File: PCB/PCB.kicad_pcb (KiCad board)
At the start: 2 copper layers, 110 x 100 mm, 53 parts, among them J1 Conn_01x03, J2 Conn_01x02, Q1 2N2907, Q10 TIP32, Q11 BD138, Q12 TIP31, Q13 2N2222, Q2 2N2907, Q3 2N2907, Q4 2N2222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

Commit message: Placmement terminé, demande de go/nogo
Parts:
- moved C6 56.9 mm to (134.0, 141.0), turned to 0 degrees
- moved Q4 41.9 mm to (106.0, 106.0)
- moved R14 39.0 mm to (90.0, 98.0), turned to 0 degrees
- moved RV2 34.4 mm to (100.0, 145.0)
- moved R9 34.2 mm to (80.0, 135.0), turned to 270 degrees
- moved R7 34.0 mm to (63.0, 129.0)
- moved Q6 32.0 mm to (89.0, 130.0)
- moved R16 32.0 mm to (116.0, 80.0), turned to 270 degrees
- moved Q7 32.0 mm to (89.0, 139.0), turned to 90 degrees
- moved C2 31.9 mm to (96.0, 104.0), turned to 270 degrees
- moved HS2 31.6 mm to (131.0, 106.0), turned to 180 degrees
- moved R3 31.4 mm to (84.0, 104.0), turned to 270 degrees
- moved R10 28.3 mm to (101.0, 128.0), turned to 270 degrees
- moved Q12 26.9 mm to (128.0, 110.0), turned to 0 degrees
- moved R8 25.3 mm to (122.0, 132.0)
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
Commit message: C10 corrigé
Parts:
- C10: value 47u -> 470u

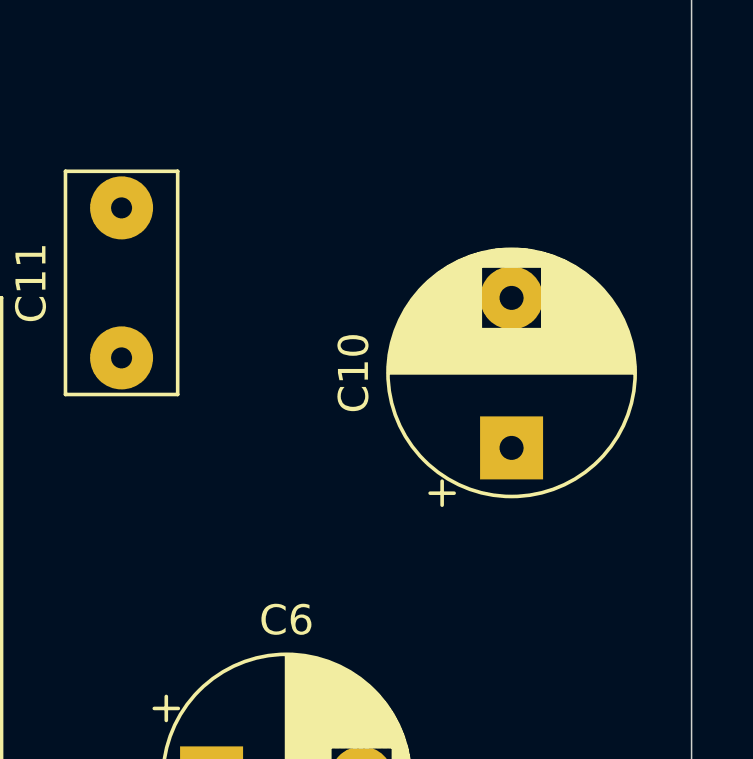
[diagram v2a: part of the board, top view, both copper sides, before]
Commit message: C8 corrigé
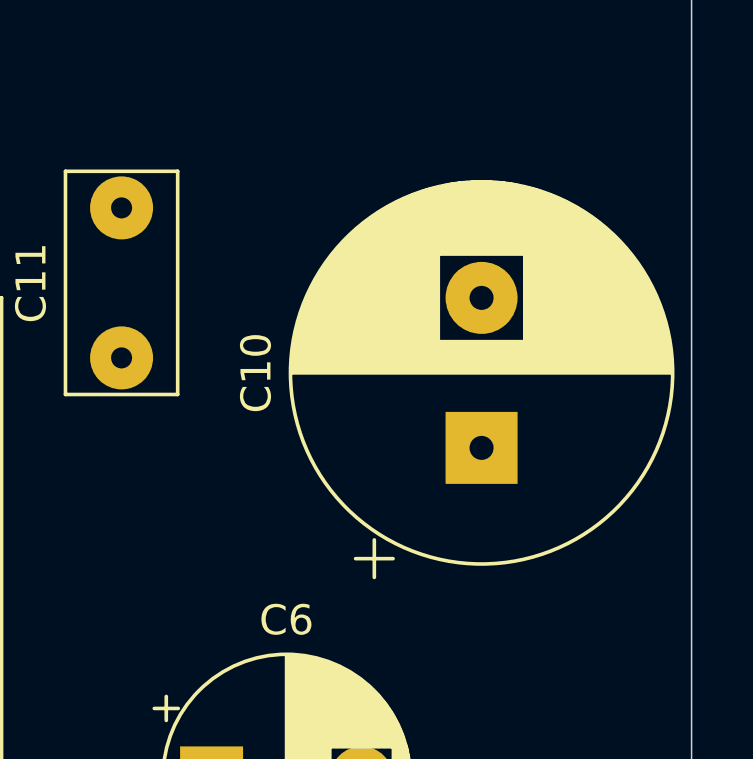
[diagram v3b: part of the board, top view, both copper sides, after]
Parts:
- C10: footprint CmpAmpliAudio:CP_Radial_D8.0mm_P5.00mm -> CmpAmpliAudio:CP_Radial_D12.5mm_P5.00mm
- moved C10 1.00 mm to (143.0, 130.0)

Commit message: routage refait en respectant vos conseils
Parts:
- removed the C8 at (53.0, 56.0)
- moved R15 92.1 mm to (144.8, 133.3), turned to 90 degrees
- moved C7 86.9 mm to (83.8, 143.5), turned to 90 degrees
- moved C4 82.1 mm to (99.1, 141.0), turned to 180 degrees
- moved C11 72.4 mm to (129.5, 54.6), turned to 270 degrees
- moved C10 65.2 mm to (143.5, 64.8), turned to 180 degrees
- moved C5 63.5 mm to (101.6, 128.3), turned to 180 degrees
- moved R14 57.9 mm to (135.9, 133.3), turned to 90 degrees
- moved Q8 56.7 mm to (128.3, 86.4), turned to 0 degrees
- moved R7 49.4 mm to (111.8, 137.2), turned to 90 degrees
- moved RV2 46.5 mm to (92.7, 99.1)
- moved C3 46.3 mm to (88.9, 110.5), turned to 180 degrees
- moved R3 43.4 mm to (44.5, 121.9)
- moved RV1 42.5 mm to (128.3, 97.8), turned to 180 degrees
- moved C6 40.0 mm to (146.1, 102.9), turned to 180 degrees
- moved Q7 39.5 mm to (125.7, 124.5)
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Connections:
- J1 pad 1: +12V -> -12V
- J1 pad 3: -12V -> +12V
- J2 pad 1: Net-(J2-Pad1) -> GND
- J2 pad 2: GND -> Net-(J2-Pad1)

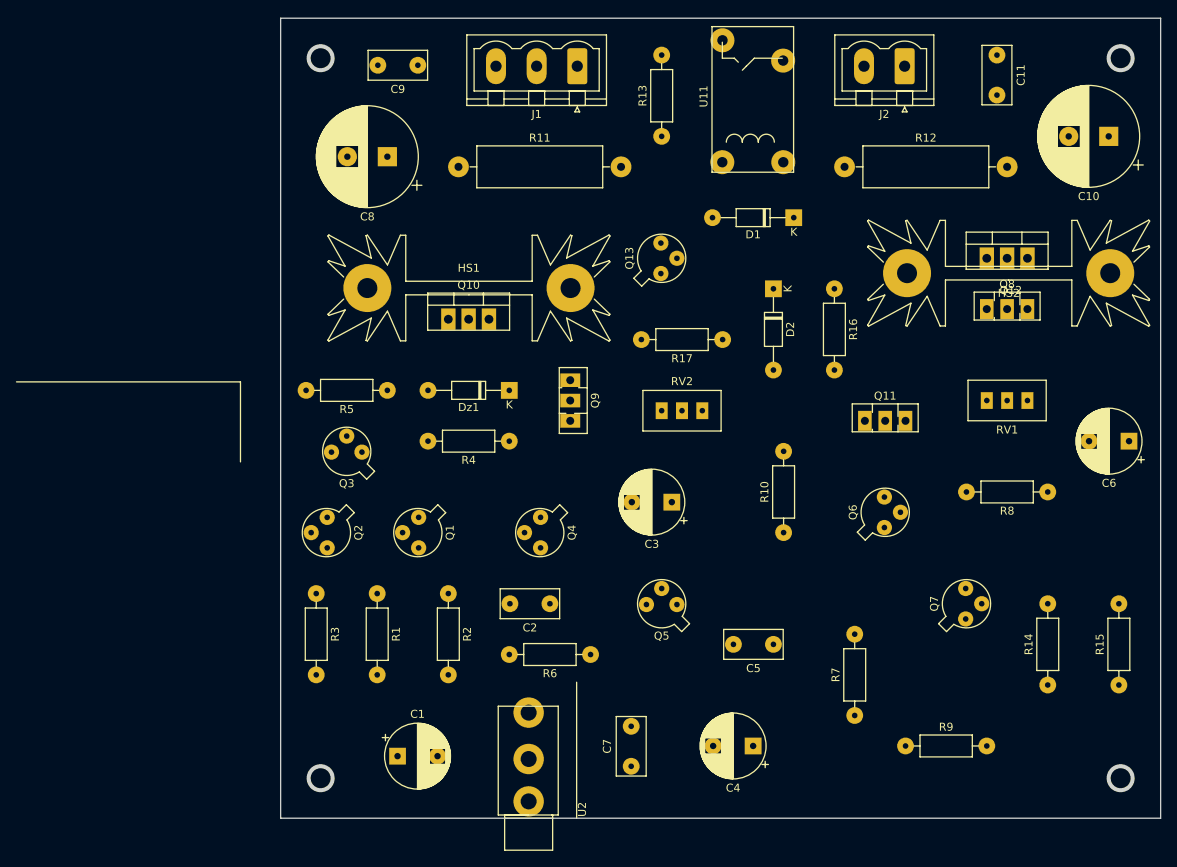
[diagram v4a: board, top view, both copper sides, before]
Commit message: routage terminé en essayant de tenir compte de vos conseils
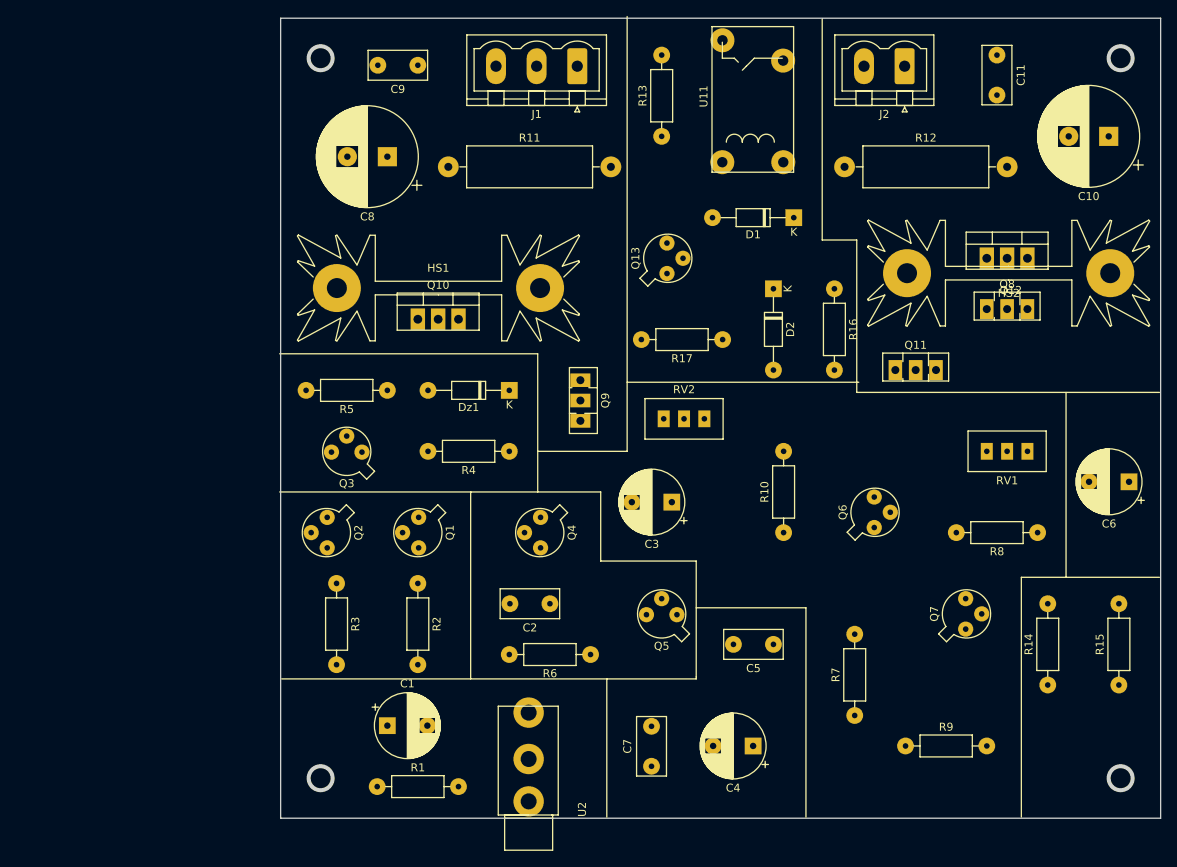
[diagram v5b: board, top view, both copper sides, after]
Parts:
- moved R1 24.1 mm to (52.1, 146.1), turned to 0 degrees
- moved Q11 7.41 mm to (116.8, 94.0)
- moved RV1 6.35 mm to (128.3, 104.1)
- moved R8 5.24 mm to (134.6, 114.3)
- moved C6 5.08 mm to (146.1, 108.0)
- moved C1 4.02 mm to (53.3, 138.4)
- moved R2 4.02 mm to (57.1, 120.7)
- moved HS1 3.81 mm to (59.7, 83.7)
- moved Q10 3.81 mm to (57.1, 87.6)
- moved R3 2.84 mm to (47.0, 120.7)
- moved C7 2.54 mm to (86.4, 143.5)
- moved Q7 1.27 mm to (125.7, 125.7)
- moved Q5 1.27 mm to (88.9, 124.5)
- moved Q6 1.27 mm to (114.3, 113.0)
- moved Q9 1.27 mm to (77.5, 95.2)
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
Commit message: routage double face
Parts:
- moved Q10 9.16 mm to (62.2, 80.0), turned to 180 degrees
- moved C11 4.02 mm to (133.3, 55.9), turned to 180 degrees
- moved U11 2.23 mm to (92.7, 62.2)
- moved J2 1.15 mm to (118.0, 57.1)
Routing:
- net GND: track 0.00 -> 476.9 mm
- net -12V: track 0.00 -> 278.9 mm
- net +12V: track 0.00 -> 198.9 mm
- net Net-(Q6-Pad3): track 0.00 -> 169.3 mm
- net Net-(R11-Pad2): track 0.00 -> 141.8 mm
- net Net-(C2-Pad1): track 0.00 -> 128.4 mm
- net Net-(Q2-Pad2): track 0.00 -> 121.9 mm
- net Net-(Q6-Pad2): track 0.00 -> 103.7 mm
- net Net-(Q7-Pad1): track 0.00 -> 45.9 mm
- net Net-(Q5-Pad1): track 0.00 -> 41.8 mm
- net Net-(C1-Pad1): track 0.00 -> 40.7 mm
- net Net-(Q10-Pad2): track 0.00 -> 37.4 mm
- net Net-(R10-Pad2): track 0.00 -> 34.8 mm
- net Net-(Q11-Pad1): track 0.00 -> 33.2 mm
- net Net-(C3-Pad1): track 0.00 -> 29.4 mm
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- added copper zone on F.Cu, net GND
